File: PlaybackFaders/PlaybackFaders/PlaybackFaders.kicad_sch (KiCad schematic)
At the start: 1 part, among them U1 Pico

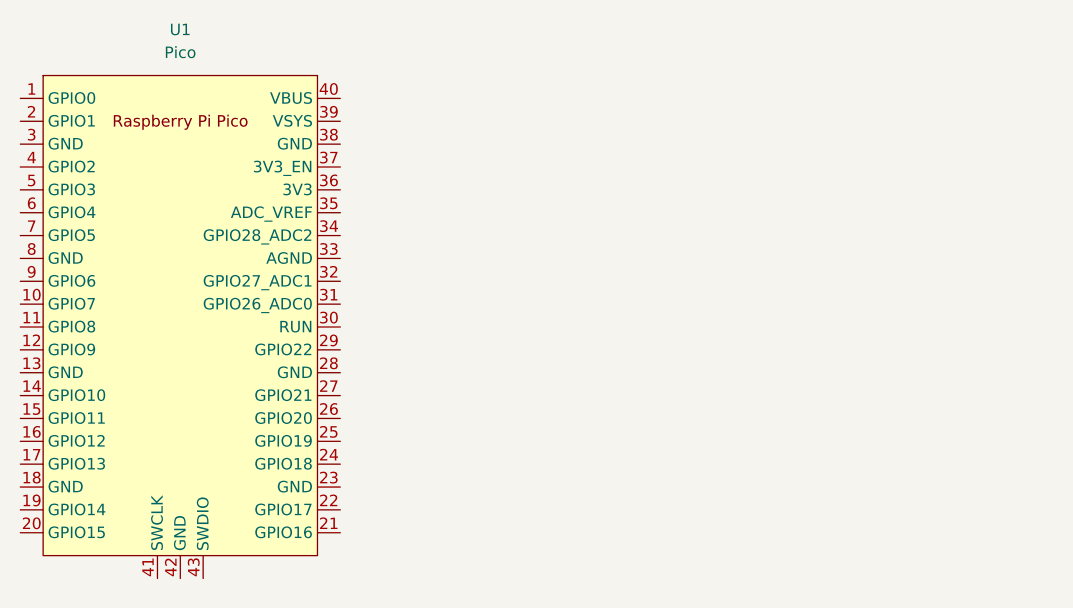
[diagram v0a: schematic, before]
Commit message: CherryMX-WS2812 added with custom symbol
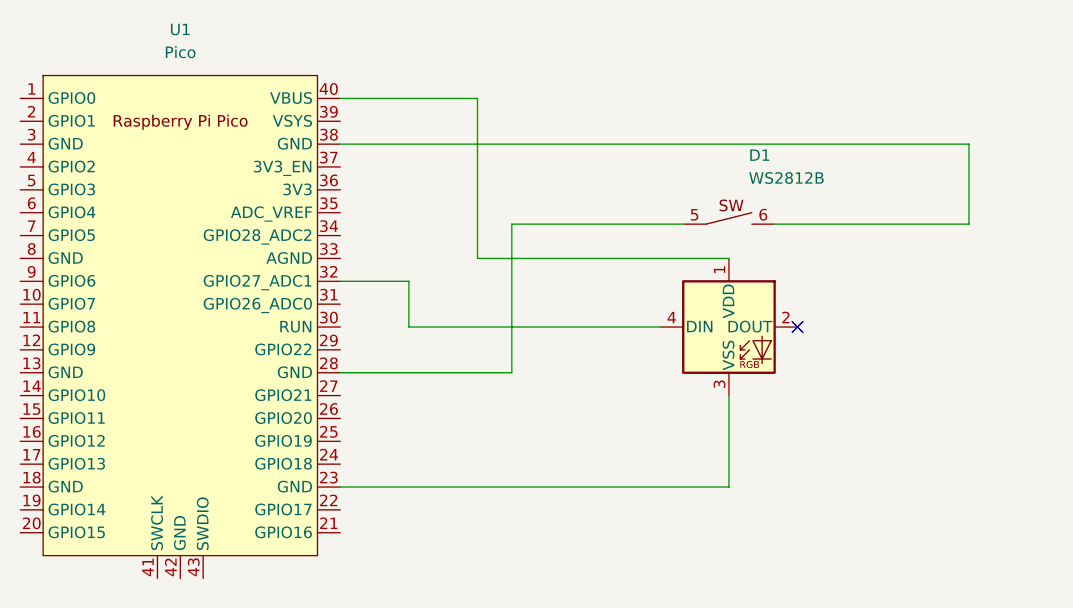
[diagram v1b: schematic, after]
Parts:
- added D1: WS2812B, Cherry_MX_SK6812_BS:Cherry_MX_SK6812_BS, symbol CherryMX_WS2812B:WS2812B
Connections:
- net at U1.23 (GND): now also D1.3 (VSS)
- net at U1.28 (GND): now also D1.5
- net at U1.32 (GPIO27_ADC1): now also D1.4 (DIN)
- net at U1.38 (GND): now also D1.6
- net at U1.40 (VBUS): now also D1.1 (VDD)
- no-connect marks 0 -> 1
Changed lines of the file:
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@@
 	(generator_version "8.0")
 	(paper "A4")
+	(no_connect
+		(at 209.55 95.25)
+	)
+	(wire
+		(pts
+			(xy 194.31 95.25) (xy 166.37 95.25)
+		)
+		(stroke
+			(width 0)
+			(type default)
+		)
+	)
+	(wire
+		(pts
+			(xy 201.93 113.03) (xy 158.75 113.03)
+		)
+		(stroke
+			(width 0)
+			(type default)
+		)
+	)
+	(wire
+		(pts
+			(xy 228.6 74.93) (xy 158.75 74.93)
+		)
+		(stroke
+			(width 0)
+			(type default)
+		)
+	)
+	(wire
+		(pts
+			(xy 201.93 87.63) (xy 173.99 87.63)
+		)
+		(stroke
+			(width 0)
+			(type default)
+		)
+	)
+	(wire
+		(pts
+			(xy 173.99 87.63) (xy 173.99 69.85)
+		)
+		(stroke
+			(width 0)
+			(type default)
+		)
+	)
+	(wire
+		(pts
+			(xy 228.6 83.82) (xy 228.6 74.93)
+		)
+		(stroke
+			(width 0)
+			(type default)
+		)
+	)
+	(wire
+		(pts
+			(xy 166.37 90.17) (xy 158.75 90.17)
+		)
+		(stroke
+			(width 0)
+			(type default)
+		)
+	)
+	(wire
+		(pts
+			(xy 177.8 100.33) (xy 158.75 100.33)
+		)
+		(stroke
+			(width 0)
+			(type default)
+		)
+	)
+	(wire
+		(pts
+			(xy 173.99 69.85) (xy 158.75 69.85)
+		)
+		(stroke
+			(width 0)
+			(type default)
+		)
+	)
+	(wire
+		(pts
+			(xy 207.01 83.82) (xy 228.6 83.82)
+		)
+		(stroke
+			(width 0)
+			(type default)
+		)
+	)
+	(wire
+		(pts
+			(xy 166.37 95.25) (xy 166.37 90.17)
+		)
+		(stroke
+			(width 0)
+			(type default)
+		)
+	)
+	(wire
+		(pts
+			(xy 196.85 83.82) (xy 177.8 83.82)
+		)
+		(stroke
+			(width 0)
+			(type default)
+		)
+	)
+	(wire
+		(pts
+			(xy 177.8 83.82) (xy 177.8 100.33)
+		)
+		(stroke
+			(width 0)
+			(type default)
+		)
+	)
+	(wire
+		(pts
+			(xy 201.93 102.87) (xy 201.93 113.03)
+		)
+		(stroke
+			(width 0)
+			(type default)
+		)
+	)
+	(symbol
+		(lib_id "CherryMX_WS2812B:WS2812B")
+		(at 201.93 95.25 0)
+		(unit 1)
+		(exclude_from_sim no)
+		(in_bom yes)
+		(on_board yes)
+		(dnp no)
+		(fields_autoplaced yes)
+		(property "Reference" "D1"
+			(at 204.1241 76.2 0)
+			(effects
+				(font
+					(size 1.27 1.27)
+				)
+				(justify left)
+			)
+		)
+		(property "Value" "WS2812B"
+			(at 204.1241 78.74 0)
+			(effects
+				(font
+					(size 1.27 1.27)
+				)
+				(justify left)
+			)
+		)
+		(property "Footprint" "Cherry_MX_SK6812_BS:Cherry_MX_SK6812_BS"
+			(at 203.2 102.87 0)
+			(effects
+				(font
+					(size 1.27 1.27)
+				)
+				(justify left top)
+				(hide yes)
+			)
+		)
+		(property "Datasheet" ""
+			(at 204.47 104.775 0)
+			(effects
+				(font
+					(size 1.27 1.27)
+				)
+				(justify left top)
+				(hide yes)
+			)
+		)
+		(property "Description" ""
+			(at 201.93 95.25 0)
+			(effects
+				(font
+					(size 1.27 1.27)
+				)
+				(hide yes)
+			)
+		)
+		(pin "3"
+		)
+		(pin "2"
+		)
+		(pin "5"
+		)
+		(pin "1"
+		)
+		(pin "4"
+		)
+		(pin "6"
+		)
+		(instances
+			(project "PlaybackFaders"
+				(path "/526de8cb-0a07-47f8-87e3-482712167997"
+					(reference "D1")
+					(unit 1)
+				)
+			)
+		)
+	)
 	(symbol
 		(lib_id "MCU_RaspberryPi_and_Boards:Pico")

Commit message: Fixed CherryMX-WS2812 pin mapping
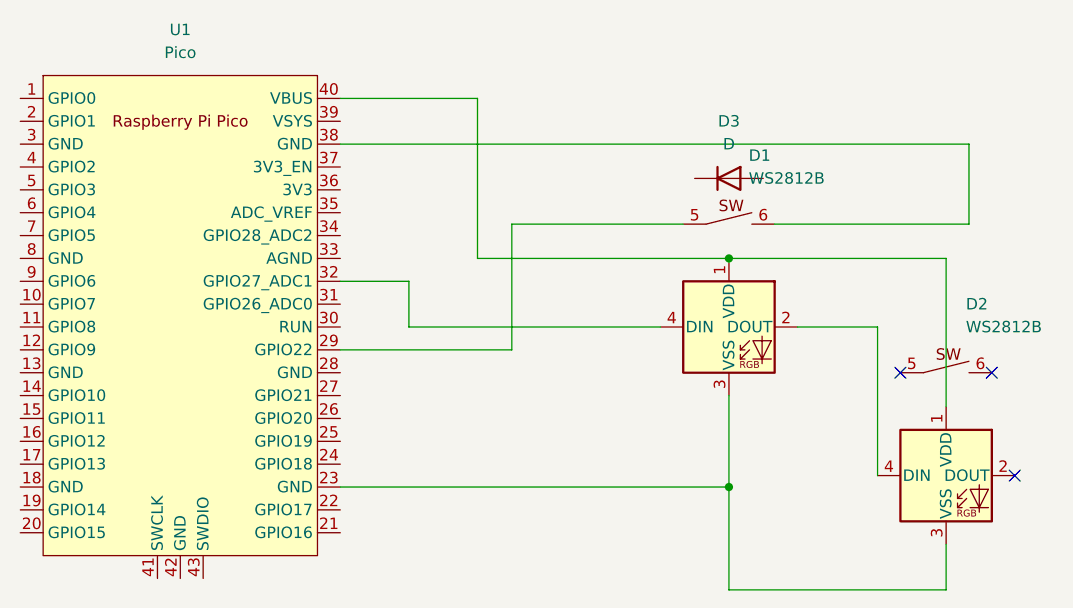
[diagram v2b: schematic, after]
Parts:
- added D2: WS2812B, Cherry_MX_WS2812:Cherry_MX_SK6812_BS, symbol CherryMX_WS2812B:WS2812B
- added D3: D, Diode_THT:D_A-405_P7.62mm_Horizontal, symbol Device:D
- D1: footprint Cherry_MX_SK6812_BS:Cherry_MX_SK6812_BS -> Cherry_MX_WS2812:Cherry_MX_SK6812_BS
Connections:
- net at D1.1 (VDD), U1.40 (VBUS): now also D2.1 (VDD)
- net at D1.2 (DOUT): now also D2.4 (DIN)
- net at D1.3 (VSS), U1.23 (GND): now also D2.3 (VSS)
- net at D1.5: now also U1.29 (GPIO22); no longer U1.28 (GND)
- no-connect marks 1 -> 3
